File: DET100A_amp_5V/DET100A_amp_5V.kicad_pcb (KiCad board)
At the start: 2 copper layers, 50 x 25 mm, 15 parts, among them J1 5227677-1, J2 Screw_Terminal_01x03, J3 5227677-1, U1 OPA656NB/250

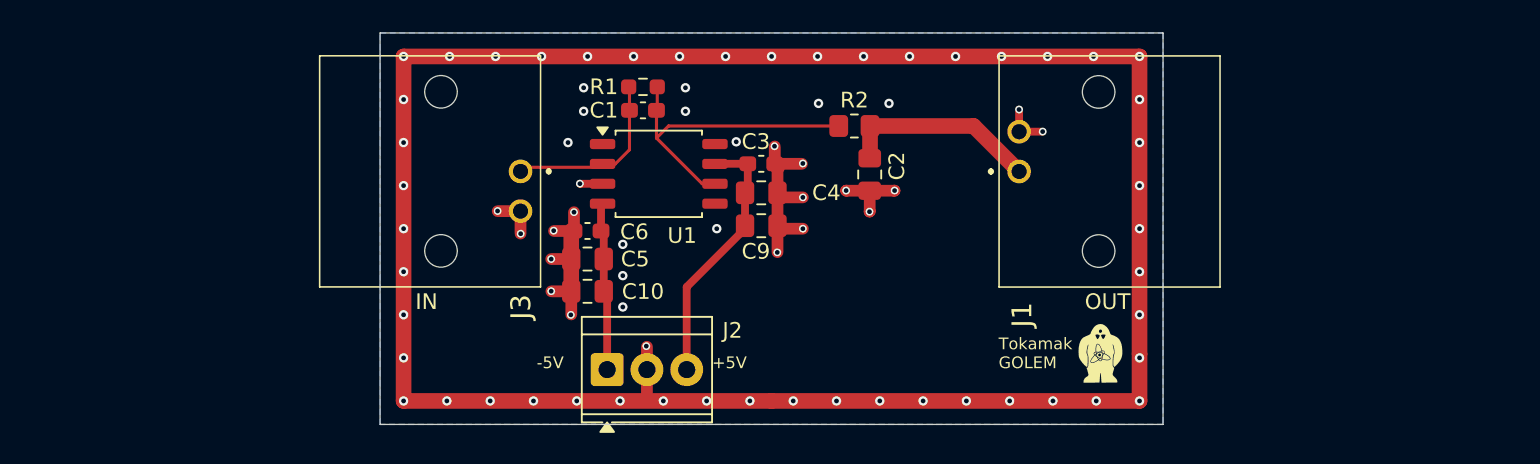
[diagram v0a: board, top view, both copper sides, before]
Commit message: feat(PCB): add TPs for the 5V version
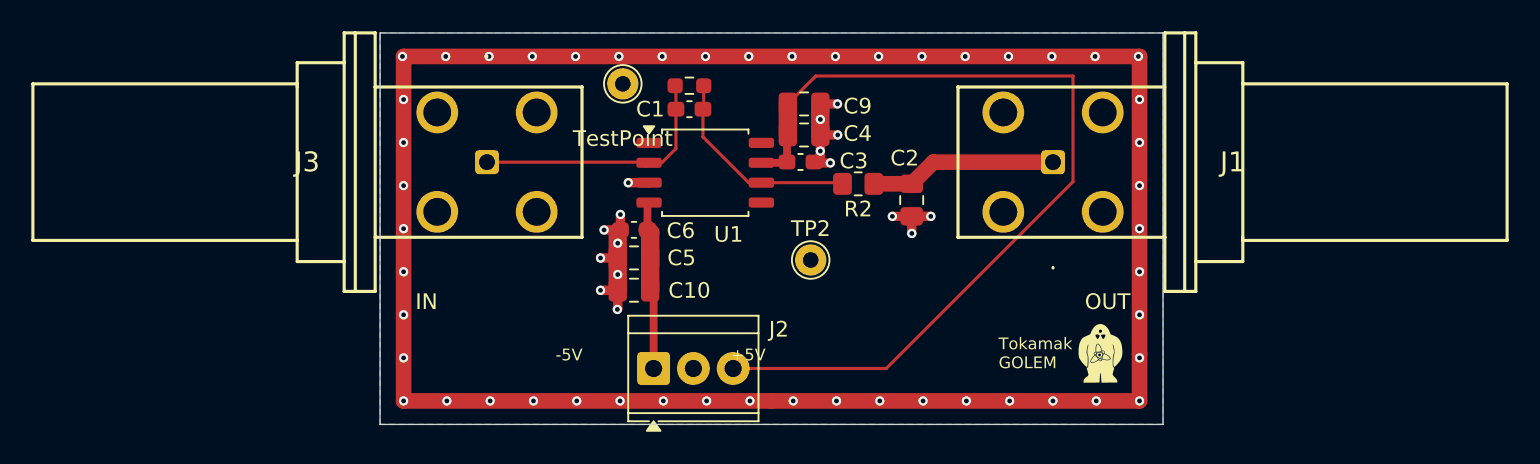
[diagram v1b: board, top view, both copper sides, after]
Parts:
- added TP1: TestPoint, Charlie:TestPoint_THTPad_D2.0mm_Drill1.0mm, F.Cu at (115.5, 78.2)
- added TP2: TestPoint, Charlie:TestPoint_THTPad_D2.0mm_Drill1.0mm, F.Cu at (127.5, 89.5)
- J1, J3: footprint 5227677-1:52276771 -> Charlie:031-6121
- moved C9 8.25 mm to (127.1, 79.5)
- moved C4 4.60 mm to (127.1, 81.5)
- moved R2 3.70 mm to (130.5, 84.6)
- moved C2 3.14 mm to (133.9, 85.7)
- moved C5 2.97 mm to (116.2, 89.4)
- moved C1 2.97 mm to (119.8, 79.9)
- moved C10 2.97 mm to (116.2, 91.4)
- moved C6 2.97 mm to (116.2, 87.6)
- moved R1 2.97 mm to (119.8, 78.4)
- moved U1 2.97 mm to (120.8, 83.9)
- moved J2 2.97 mm to (117.5, 96.4)
- moved C3 2.51 mm to (126.8, 83.2)
- moved J1 2.25 mm to (143.0, 83.2), turned to 0 degrees
- moved J3 2.22 mm to (106.8, 83.2), turned to 180 degrees
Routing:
- net Net-(J2-Pin_1): track 16.9 -> 57.7 mm
- net GND: track 175.7 -> 159.3 mm, vias 80 -> 66
- net Net-(U1-OUTPUT): track 20.2 -> 13.4 mm
- net Net-(J3-In): track 11.8 -> 17.1 mm
- net Net-(J1-In): track 12.8 -> 12.0 mm
